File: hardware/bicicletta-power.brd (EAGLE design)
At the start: 160 x 100 mm, 23 parts, among them IC1 LM5017, IC2 LM1117-3.3

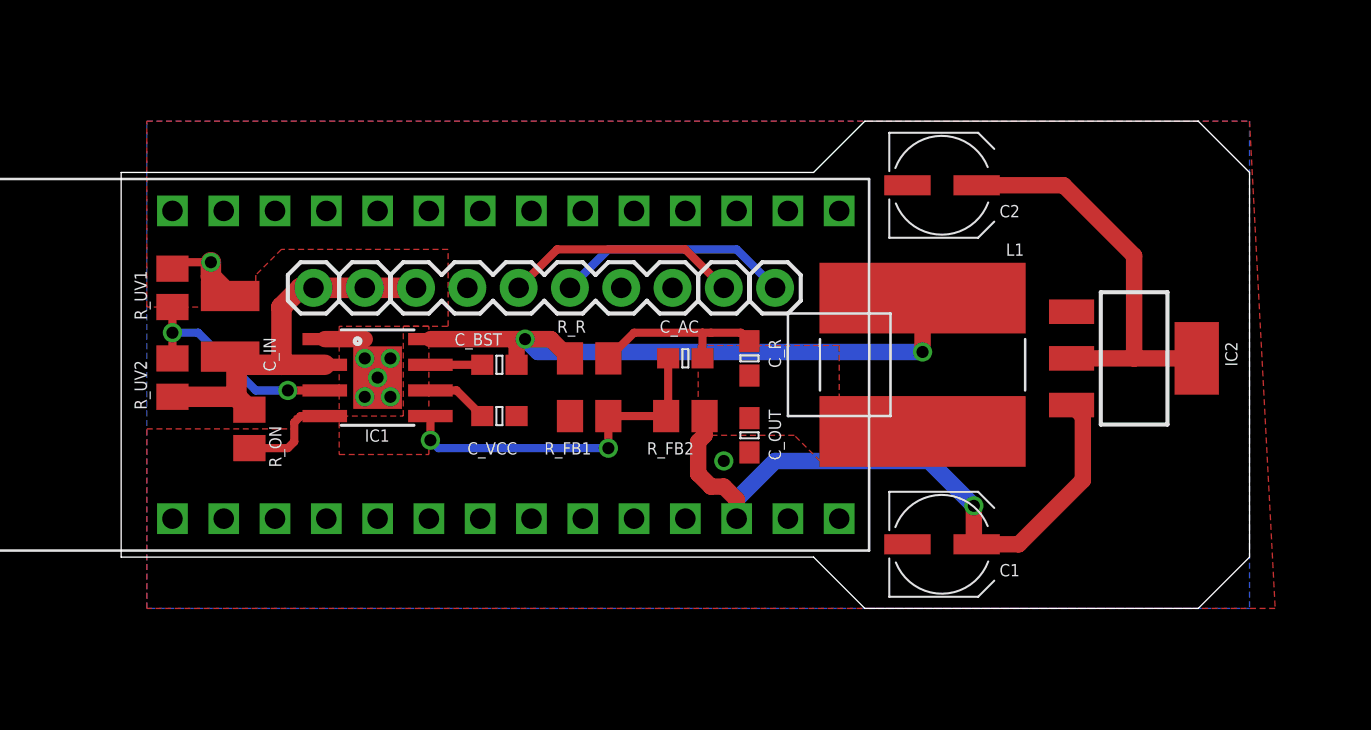
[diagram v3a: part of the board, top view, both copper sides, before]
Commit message: Why not use the Blend's 150mA 3.3V regulator?
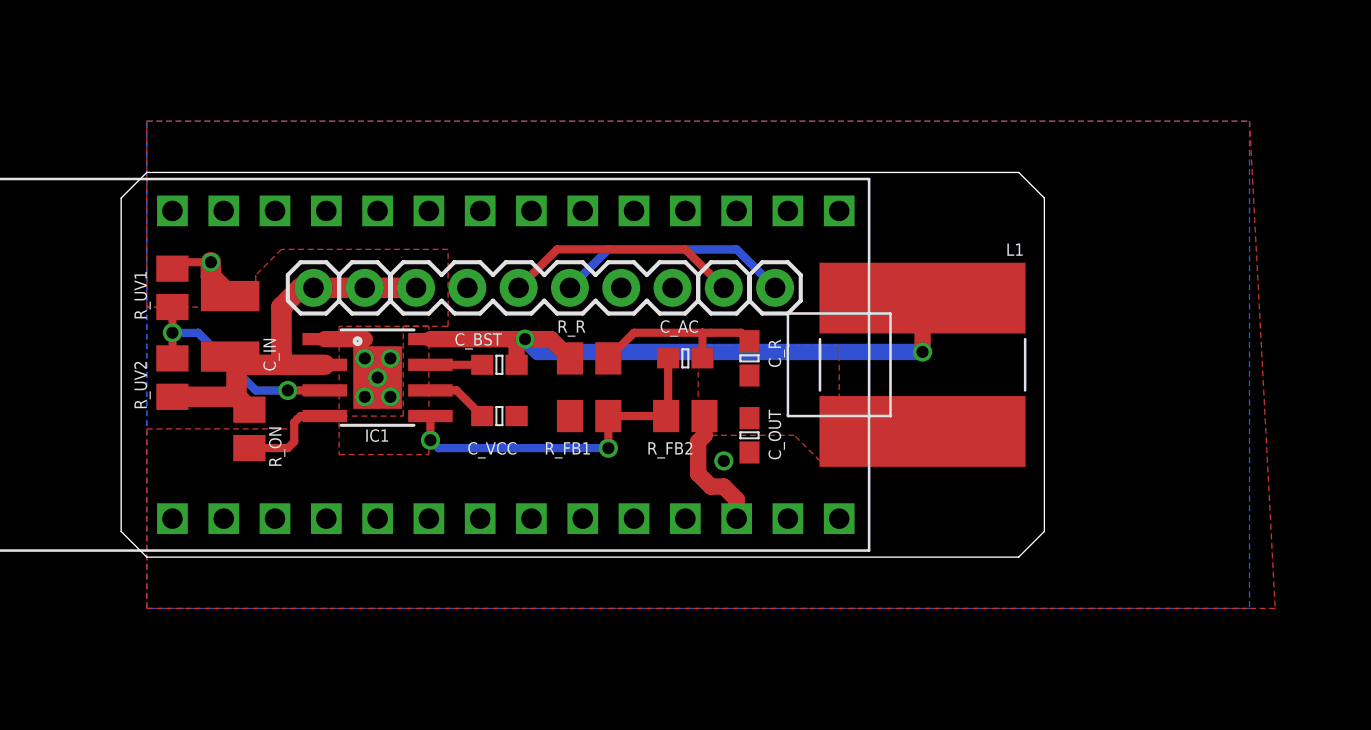
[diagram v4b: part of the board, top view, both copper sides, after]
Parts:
- removed C1, C2: 14uF, rcl:UD-5X5,8_NICHICON
- removed IC2: LM1117-3.3, SparkFun-PowerIC:SOT223
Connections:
- net 3.3V: now also U$1.P$16; no longer C2.+, IC2.2, IC2.4
- net 5V: no longer C1.+, IC2.3
- net GND: no longer C1.-, C2.-, IC2.1
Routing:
- net 5V: track 33.4 -> 6.37 mm, vias 1 -> 0
- net 3.3V: track 20.5 -> 0.00 mm
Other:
- outline, holes or cut-outs redrawn
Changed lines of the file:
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@@
 <wire x1="160" y1="100" x2="0" y2="100" width="0" layer="20"/>
 <wire x1="0" y1="100" x2="0" y2="0" width="0" layer="20"/>
-<wire x1="40.64" y1="83.82" x2="74.93" y2="83.82" width="0" layer="20"/>
-<wire x1="74.93" y1="83.82" x2="77.47" y2="86.36" width="0" layer="20"/>
-<wire x1="77.47" y1="86.36" x2="93.98" y2="86.36" width="0" layer="20"/>
-<wire x1="93.98" y1="86.36" x2="96.52" y2="83.82" width="0" layer="20"/>
-<wire x1="96.52" y1="83.82" x2="96.52" y2="64.77" width="0" layer="20"/>
-<wire x1="96.52" y1="64.77" x2="93.98" y2="62.23" width="0" layer="20"/>
-<wire x1="93.98" y1="62.23" x2="77.47" y2="62.23" width="0" layer="20"/>
-<wire x1="77.47" y1="62.23" x2="74.93" y2="64.77" width="0" layer="20"/>
-<wire x1="74.93" y1="64.77" x2="40.64" y2="64.77" width="0" layer="20"/>
-<wire x1="40.64" y1="83.82" x2="40.64" y2="64.77" width="0" layer="20"/>
+<wire x1="40.64" y1="82.55" x2="41.91" y2="83.82" width="0" layer="20"/>
+<wire x1="41.91" y1="83.82" x2="85.09" y2="83.82" width="0" layer="20"/>
+<wire x1="85.09" y1="83.82" x2="86.36" y2="82.55" width="0" layer="20"/>
+<wire x1="86.36" y1="82.55" x2="86.36" y2="66.04" width="0" layer="20"/>
+<wire x1="86.36" y1="66.04" x2="85.09" y2="64.77" width="0" layer="20"/>
+<wire x1="85.09" y1="64.77" x2="41.91" y2="64.77" width="0" layer="20"/>
+<wire x1="41.91" y1="64.77" x2="40.64" y2="66.04" width="0" layer="20"/>
+<wire x1="40.64" y1="82.55" x2="40.64" y2="66.04" width="0" layer="20"/>
 </plain>
 <attributes>
@@
 <attribute name="VALUE" x="62.5475" y="72.0725" size="1.27" layer="27"/>
 </element>
-<element name="IC2" library="SparkFun-PowerIC" package="SOT223" value="LM1117-3.3" x="90.805" y="74.6125" smashed="yes" rot="R270">
-<attribute name="NAME" x="95.3135" y="75.438" size="0.6096" layer="25" rot="R270"/>
-<attribute name="VALUE" x="90.6145" y="75.692" size="0.4064" layer="27" rot="R270"/>
-</element>
-<element name="C1" library="rcl" package="UD-5X5,8_NICHICON" value="14uF" x="81.28" y="65.405" smashed="yes">
-<attribute name="NAME" x="84.1375" y="63.8175" size="0.6096" layer="25"/>
-<attribute name="VALUE" x="78.74" y="61.595" size="1.016" layer="27"/>
-</element>
-<element name="C2" library="rcl" package="UD-5X5,8_NICHICON" value="14uF" x="81.28" y="83.185" smashed="yes">
-<attribute name="NAME" x="84.1375" y="81.5975" size="0.6096" layer="25"/>
-<attribute name="VALUE" x="78.74" y="79.375" size="1.016" layer="27"/>
-</element>
 <element name="C_R" library="rcl" package="C0603" value="3300pF" x="71.755" y="74.6125" smashed="yes" rot="R270">
 <attribute name="NAME" x="72.7075" y="75.565" size="0.6096" layer="25" rot="R270"/>
@@
 <contactref element="C_VCC" pad="2"/>
 <contactref element="R_FB1" pad="1"/>
-<contactref element="IC2" pad="1"/>
-<contactref element="C2" pad="-"/>
-<contactref element="C1" pad="-"/>
 <contactref element="JP3" pad="2"/>
 <polygon width="0.4064" layer="16" isolate="0.3048">
@@
 </signal>
 <signal name="5V">
-<contactref element="IC2" pad="3"/>
-<contactref element="C1" pad="+"/>
 <contactref element="C_OUT" pad="1"/>
 <polygon width="0.4064" layer="1" thermals="no">
@@
 <contactref element="C_R" pad="2"/>
 <contactref element="U$1" pad="P$12"/>
-<wire x1="83.005" y1="65.405" x2="85.09" y2="65.405" width="0.8128" layer="1"/>
-<wire x1="85.09" y1="65.405" x2="88.265" y2="68.58" width="0.8128" layer="1"/>
-<wire x1="88.265" y1="68.58" x2="88.265" y2="71.755" width="0.8128" layer="1"/>
-<wire x1="88.265" y1="71.755" x2="87.63" y2="72.39" width="0.8128" layer="1"/>
-<wire x1="73.025" y1="69.5325" x2="80.645" y2="69.5325" width="0.8128" layer="16"/>
-<wire x1="80.645" y1="69.5325" x2="82.8675" y2="67.31" width="0.8128" layer="16"/>
-<via x="82.8675" y="67.31" extent="1-16" drill="0.6"/>
-<wire x1="82.8675" y1="67.31" x2="82.8675" y2="65.5425" width="0.8128" layer="1"/>
-<wire x1="82.8675" y1="65.5425" x2="83.005" y2="65.405" width="0.8128" layer="1"/>
-<wire x1="73.025" y1="69.5325" x2="71.12" y2="67.6275" width="0.8128" layer="16"/>
-<wire x1="71.12" y1="67.6275" x2="71.12" y2="66.675" width="0.8128" layer="16"/>
 <wire x1="69.53" y1="71.755" x2="69.53" y2="70.8" width="0.8128" layer="1"/>
 <wire x1="69.53" y1="70.8" x2="69.215" y2="70.485" width="0.8128" layer="1"/>
@@
 <wire x1="69.215" y1="68.8975" x2="69.85" y2="68.2625" width="0.8128" layer="1"/>
 <wire x1="69.85" y1="68.2625" x2="70.485" y2="68.2625" width="0.8128" layer="1"/>
-<wire x1="87.63" y1="72.39" x2="87.7062" y2="72.3011" width="0" layer="19" extent="1-1"/>
 </signal>
 <signal name="N$1">
@@
 <wire x1="43.18" y1="75.8825" x2="43.18" y2="77.155" width="0" layer="19" extent="1-1"/>
 </signal>
-<signal name="3.3V">
-<contactref element="IC2" pad="4"/>
-<contactref element="IC2" pad="2"/>
-<contactref element="C2" pad="+"/>
-<wire x1="93.904" y1="74.6125" x2="90.805" y2="74.6125" width="0.8128" layer="1"/>
-<wire x1="90.805" y1="74.6125" x2="87.7062" y2="74.6125" width="0.8128" layer="1"/>
-<wire x1="83.005" y1="83.185" x2="87.3125" y2="83.185" width="0.8128" layer="1"/>
-<wire x1="87.3125" y1="83.185" x2="90.805" y2="79.6925" width="0.8128" layer="1"/>
-<wire x1="90.805" y1="74.6125" x2="90.805" y2="79.6925" width="0.8128" layer="1"/>
-</signal>
 <signal name="N$4">
 <contactref element="IC1" pad="8"/>
@@
 <contactref element="U$1" pad="P$17"/>
 </signal>
+<signal name="3.3V">
+<contactref element="U$1" pad="P$16"/>
+</signal>
 </signals>
-<errors>
-</errors>
 </board>
 </drawing>

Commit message: There it is. Order that.
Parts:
- removed C_AC: 100nF, rcl:C0603
- removed C_BST: 0.01uF, rcl:C0603
- removed C_R: 3300pF, rcl:C0603
- removed C_VCC: 1uF, rcl:C0603
- removed JP4, JP5, JP6, JP7: M01PTH, SparkFun-Connectors:1X01
- removed R_ON: 250K, rcl:M0805
- removed R_R: 2M, rcl:M0805
- removed R_UV1: 14K, rcl:M0805
- removed R_UV2: 125K, rcl:M0805
- added C_BOOT: 22nF, rcl:C0603
- added C_BYP: 1uF, rcl:C0603
- added C_COMP: 1.8nF, rcl:C0603
- added C_RAMP: 470pF, rcl:C0603
- added C_SS: 1nF, rcl:C0603
- added D1: DFLS1100-7, TI:POWERDI123
- added JP1: (no value), SparkFun-Connectors:1X06
- added R_COMP: 19K1, rcl:R0603
- added R_T: 10K7 75V, rcl:R0603
- C_IN: value 2.2uF -> 1uF; device rcl:C1210K -> rcl:C1206
- C_OUT: value 5.6uF -> 10uF; device rcl:C0603 -> rcl:C0805
- IC1: value LM5017 -> LM5574MT/NOPB; device Railstars:SOIC-8-POWERPAD -> TI:MTC16
- L1: value 100uH -> SRN6045-101M; device Railstars:SRN1060 -> TI:SRN6045
- R_FB1: device rcl:M0805 -> rcl:R0603
- R_FB2: value 3K -> 3K09; device rcl:M0805 -> rcl:R0603
- moved JP3 14.8 mm to (40.6, 80.6), turned to 270 degrees
- moved L1 10.9 mm to (69.8, 77.5)
- moved C_OUT 5.28 mm to (76.2, 73.7)
- moved R_FB1 4.85 mm to (59.7, 69.2)
- moved U$1 3.81 mm to (59.7, 74.3)
- moved R_FB2 2.84 mm to (67.3, 69.2), turned to 180 degrees
- moved C_IN 2.56 mm to (48.3, 77.5), turned to 270 degrees
- moved IC1 2.54 mm to (55.9, 73.7), turned to 0 degrees
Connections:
- removed net N$4: C_BST.2, IC1.8, L1.P$1, R_R.1
- new net N$10: C_BOOT.1, IC1.16
- new net N$11: C_BOOT.2, D1.K, IC1.14, IC1.15, L1.1
- new net N$5: IC1.7, R_T.1
- new net N$8: IC1.5, R_COMP.1
- net 5V: now also IC1.11, L1.2; no longer C_R.2, L1.P$2
- net GND: now also C_BYP.2, C_RAMP.2, C_SS.2, IC1.12, IC1.9, JP1.2, R_T.2; no longer C_VCC.2, IC1.1, IC1.P$1, R_UV1.1
- net N$1: now also C_SS.1, IC1.10; no longer IC1.4, R_ON.2
- net N$2: now also C_BYP.1, IC1.1; no longer C_AC.2, IC1.5, R_FB1.2, R_FB2.1
- net N$3: now also C_RAMP.1, IC1.8; no longer IC1.3, R_UV1.2, R_UV2.2
- net N$6: now also C_COMP.2, IC1.6, R_FB1.2, R_FB2.1; no longer C_AC.1, C_R.1, R_R.2
- net N$7: now also C_COMP.1, R_COMP.2; no longer C_BST.1, IC1.7
- net N$9: now also D1.A, IC1.13; no longer C_VCC.1, IC1.6
- net SHUNT+: now also JP1.4; no longer JP4.1
- net SHUNT-: now also JP1.3; no longer JP5.1
- net SPEED_5: now also JP1.5
- net THROTTLE_OUT_5: now also JP1.6
- net V_BATT: now also IC1.3, JP1.1; no longer IC1.2, JP6.1, JP7.1, R_ON.1, R_UV2.1
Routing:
- net N$4: track 31.2 -> 0.00 mm, vias 2 -> 0
- net N$6: track 8.96 -> 30.4 mm, vias 0 -> 3
- net 5V: track 6.37 -> 25.5 mm, vias 0 -> 8
- net V_BATT: track 21.0 -> 5.35 mm
- net N$2: track 17.5 -> 3.80 mm, vias 2 -> 0
- net GND: track 7.23 -> 18.4 mm, vias 7 -> 8
- net SHUNT+: track 11.7 -> 2.54 mm
- net SHUNT-: track 11.7 -> 2.54 mm
- net N$8: track 0.00 -> 7.83 mm
- net N$3: track 11.3 -> 3.74 mm, vias 2 -> 0
- net N$5: track 0.00 -> 4.16 mm
- net THROTTLE_OUT_5: track 0.00 -> 2.54 mm
- net SPEED_5: track 0.00 -> 2.54 mm
- net N$9: track 3.09 -> 5.49 mm
- net N$10: track 0.00 -> 2.35 mm
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- added copper zone on layer 16, net 5V
- added copper zone on layer 1, net N$11
- added copper zone on layer 16, net N$11
- added copper zone on layer 1, net N$9
- added copper zone on layer 1, net V_BATT
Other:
- outline, holes or cut-outs redrawn
- board text added: "S+"
- board text added: "S-"
- board text added: "Sp"
- board text added: "Th"
- board text added: "V+"
- board text added: "V-"

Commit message: Finalizations.
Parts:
- moved C_BOOT 74.5 mm to (23.2, 13.3)
- moved C_BYP 74.5 mm to (19.1, 13.3)
- moved C_COMP 74.5 mm to (11.7, 6.35)
- moved C_RAMP 74.5 mm to (19.1, 4.45)
- moved C_SS 74.5 mm to (26.7, 4.45)
- moved D1 74.5 mm to (26.7, 9.21)
- moved R_COMP 74.5 mm to (9.21, 6.35)
- moved R_FB1 74.5 mm to (22.9, 4.45)
- moved R_FB2 74.5 mm to (30.5, 4.45)
- moved R_T 74.5 mm to (15.2, 4.45)
- moved C_OUT 74.5 mm to (39.4, 8.89)
- moved C_IN 74.5 mm to (11.4, 12.7)
- moved IC1 74.5 mm to (19.1, 8.89)
- moved JP1 74.5 mm to (6.35, 15.9)
- moved JP3 74.5 mm to (3.81, 15.9)
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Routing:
- net V_BATT: track 5.35 -> 6.98 mm
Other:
- board size 160 x 100 mm -> 45.7 x 19.1 mm
- board text added: "bicicletta power 20141113"

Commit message: Final silkscreen
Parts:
- added U$2: (no value), Artificial Science:RAILSTARS_25MM
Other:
- board text added: "20141113"
- board text added: "bicicletta power"
- board text removed: "bicicletta power 20141113"
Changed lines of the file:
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@@
 <text x="1.5875" y="5.08" size="0.6096" layer="22" rot="MR90">Sp</text>
 <text x="1.5875" y="2.8575" size="0.6096" layer="22" rot="MR90">Th</text>
-<text x="44.45" y="5.08" size="1.016" layer="22" rot="MR0">bicicletta power 20141113</text>
+<text x="44.45" y="3.175" size="1.016" layer="22" rot="MR0">bicicletta power</text>
 <text x="2.2225" y="15.5575" size="0.6096" layer="21" rot="R90">V+</text>
 <text x="2.2225" y="13.0175" size="0.6096" layer="21" rot="R90">V-</text>
@@
 <text x="2.2225" y="5.08" size="0.6096" layer="21" rot="R90">Sp</text>
 <text x="2.2225" y="2.8575" size="0.6096" layer="21" rot="R90">Th</text>
+<text x="6.985" y="0.635" size="0.6096" layer="22" rot="MR0">20141113</text>
 </plain>
 <attributes>
@@
 <attribute name="VALUE" x="3.175" y="17.145" size="1.27" layer="27" rot="R270"/>
 </element>
+<element name="U$2" library="Artificial Science" package="RAILSTARS_25MM" value="" x="44.45" y="5.08" rot="MR0"/>
 </elements>
 <signals>
